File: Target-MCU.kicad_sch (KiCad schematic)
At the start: 18 parts, among them Q6 DMG1012UW-7, SW5 12V 50mA, U4 CH32V003F4P6

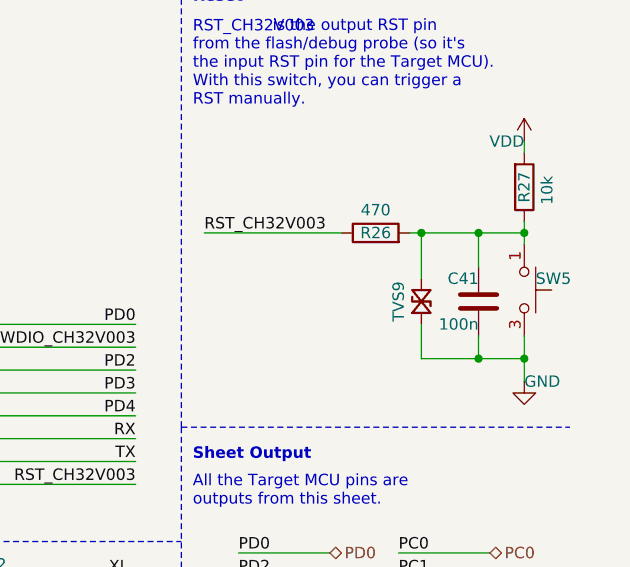
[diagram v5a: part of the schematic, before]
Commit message: Replace TVS `SP1007-01ETG` with `LESD8LH5.0CT5G`
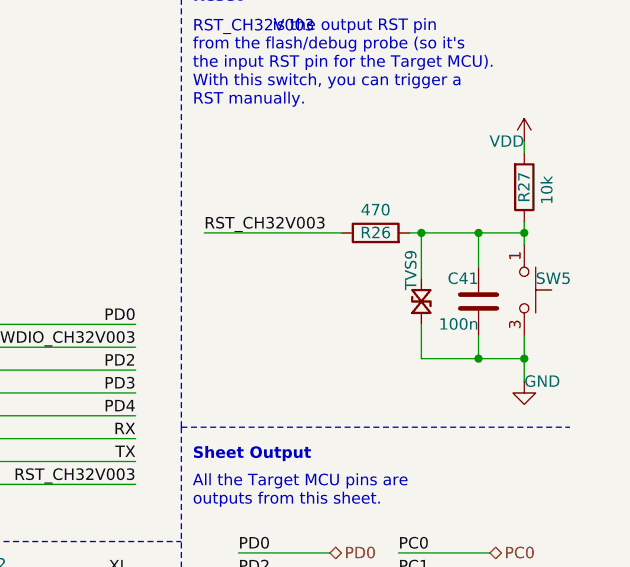
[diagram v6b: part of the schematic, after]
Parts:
- removed TVS9: 5V, Tiny_Scarab:D_SOD-882_SP1007-01ETG, symbol Tiny_Scarab:TVS_SP1007-01ETG
- added TVS9: 5V, Tiny_Scarab:D_SOD-882_SP1007-01ETG, symbol Tiny_Scarab:TVS_LESD8LH5.0CT5G
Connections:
- net GND: now also TVS9.2
- net at C41.1, R26.2, R27.1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: now also TVS9.1
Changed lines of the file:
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@@
-	)
-	(symbol
-		(lib_id "Tiny_Scarab:TVS_SP1007-01ETG")
-		(at 180.34 55.88 0)
-		(unit 1)
-		(exclude_from_sim no)
-		(in_bom yes)
-		(on_board yes)
-		(dnp no)
-		(property "Reference" "TVS9"
-			(at 177.8 55.88 90)
-			(effects
-				(font
-					(size 1.27 1.27)
-				)
-			)
-		)
-		(property "Value" "5V"
-			(at 179.07 57.15 0)
-			(effects
-				(font
-					(size 1.27 1.27)
-				)
-				(justify right)
-				(hide yes)
-			)
-		)
-		(property "Footprint" "Tiny_Scarab:D_SOD-882_SP1007-01ETG"
-			(at 180.34 33.02 0)
-			(effects
-				(font
-					(size 1.27 1.27)
-				)
-				(justify bottom)
-				(hide yes)
-			)
-		)
-		(property "Datasheet" ""
-			(at 168.91 41.91 0)
-			(effects
-				(font
-					(size 1.27 1.27)
-				)
-				(justify left)
-				(hide yes)
-			)
-		)
-		(property "Description" "TVS bidirectional, 6V, 3.5pF"
-			(at 180.34 55.88 0)
-			(effects
-				(font
-					(size 1.27 1.27)
-				)
-				(hide yes)
-			)
-		)
-		(property "Manufacturer" "Littelfuse"
-			(at 180.34 35.56 0)
-			(effects
-				(font
-					(size 1.27 1.27)
-				)
-				(justify bottom)
-				(hide yes)
-			)
-		)
-		(property "MPN" "SP1007-01ETG"
-			(at 180.34 38.1 0)
-			(effects
-				(font
-					(size 1.27 1.27)
-				)
-				(justify bottom)
-				(hide yes)
-			)
-		)
-		(property "JLCPCB Part #" "C126836"
-			(at 180.34 39.37 0)
-			(effects
-				(font
-					(size 1.27 1.27)
-				)
-				(hide yes)
-			)
-		)
-		(property "DigiKey" "F6187TR-ND"
-			(at 180.34 41.91 0)
-			(effects
-				(font
-					(size 1.27 1.27)
-				)
-				(hide yes)
-			)
-		)
-		(property "Farnell" "2777317"
-			(at 180.34 44.45 0)
-			(effects
-				(font
-					(size 1.27 1.27)
-				)
-				(hide yes)
-			)
-		)
-		(property "Mouser" "576-SP1007-01ETG"
-			(at 180.34 46.99 0)
-			(effects
-				(font
-					(size 1.27 1.27)
-				)
-				(hide yes)
-			)
-		)
-		(pin "1"
-		)
-		(pin "2"
-		)
-		(instances
-			(project "tiny-scarab"
-				(path "/156c5422-ee07-49a4-8263-a2dbd26b90bd/d0c4b0c3-1e7e-4a4c-add3-8d4a3a10843d"
-					(reference "TVS9")
-					(unit 1)
-				)
-			)
-		)
 	)
 	(symbol
@@
 					(unit 1)
 				)
+			)
+		)
+	)
+	(symbol
+		(lib_id "Tiny_Scarab:TVS_LESD8LH5.0CT5G")
+		(at 180.34 55.88 0)
+		(unit 1)
+		(exclude_from_sim no)
+		(in_bom yes)
+		(on_board yes)
+		(dnp no)
+		(property "Reference" "TVS9"
+			(at 179.197 54.61 90)
+			(effects
+				(font
+					(size 1.27 1.27)
+				)
+				(justify left)
+			)
+		)
+		(property "Value" "5V"
+			(at 182.88 57.1499 0)
+			(effects
+				(font
+					(size 1.27 1.27)
+				)
+				(justify left)
+				(hide yes)
+			)
+		)
+		(property "Footprint" "Tiny_Scarab:D_SOD-882_SP1007-01ETG"
+			(at 180.086 38.608 0)
+			(effects
+				(font
+					(size 1.27 1.27)
+				)
+				(justify bottom)
+				(hide yes)
+			)
+		)
+		(property "Datasheet" ""
+			(at 168.656 47.498 0)
+			(effects
+				(font
+					(size 1.27 1.27)
+				)
+				(justify left)
+				(hide yes)
+			)
+		)
+		(property "Description" "TVS bidirectional, 5V, 2.7-3.5pF"
+			(at 180.086 46.99 0)
+			(effects
+				(font
+					(size 1.27 1.27)
+				)
+				(hide yes)
+			)
+		)
+		(property "Manufacturer" "UMW(Youtai Semiconductor Co., Ltd.)"
+			(at 180.086 41.148 0)
+			(effects
+				(font
+					(size 1.27 1.27)
+				)
+				(justify bottom)
+				(hide yes)
+			)
+		)
+		(property "MPN" "LESD8LH5.0CT5G"
+			(at 180.086 43.688 0)
+			(effects
+				(font
+					(size 1.27 1.27)
+				)
+				(justify bottom)
+				(hide yes)
+			)
+		)
+		(property "JLCPCB Part #" "C3001954"
+			(at 180.086 44.958 0)
+			(effects
+				(font
+					(size 1.27 1.27)
+				)
+				(hide yes)
+			)
+		)
+		(property "DigiKey" ""
+			(at 180.086 47.498 0)
+			(effects
+				(font
+					(size 1.27 1.27)
+				)
+				(hide yes)
+			)
+		)
+		(property "Farnell" ""
+			(at 180.34 42.418 0)
+			(effects
+				(font
+					(size 1.27 1.27)
+				)
+				(hide yes)
+			)
+		)
+		(property "Mouser" ""
+			(at 180.34 44.958 0)
+			(effects
+				(font
+					(size 1.27 1.27)
+				)
+				(hide yes)
+			)
+		)
+		(pin "2"
+		)
+		(pin "1"
+		)
+		(instances
+			(project "tiny-scarab"
+				(path "/156c5422-ee07-49a4-8263-a2dbd26b90bd/d0c4b0c3-1e7e-4a4c-add3-8d4a3a10843d"
+					(reference "TVS9")
+					(unit 1)
+				)

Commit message: Fix R28
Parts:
- R28: JLCPCB Part # (none) -> C11702; MPN GPR04021K -> 0402WGF1001TCE; Manufacturer (none) -> UNI-ROYAL(Uniroyal Elec)
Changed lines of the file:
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@@
 			)
 		)
-		(property "MPN" "GPR04021K"
+		(property "Manufacturer" "UNI-ROYAL(Uniroyal Elec)"
 			(at 29.21 109.22 0)
 			(effects
 				(font
+					(size 1.27 1.27)
+				)
+				(hide yes)
+			)
+		)
+		(property "MPN" "0402WGF1001TCE"
+			(at 29.21 109.22 90)
+			(effects
+				(font
+					(size 1.27 1.27)
+				)
+				(hide yes)
+			)
+		)
+		(property "JLCPCB Part #" "C11702"
+			(at 29.21 109.22 90)
+			(effects
+				(font
